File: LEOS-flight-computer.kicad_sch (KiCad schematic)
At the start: 20 parts, among them J1 MicroFit_1x4, J2 MicroFit_1x4, J3 GPIO, J4 I2C Breakout, J5 SPI Breakout, U1 MCP2562FD, U2 MCP2518FD, Y1 40 MHz

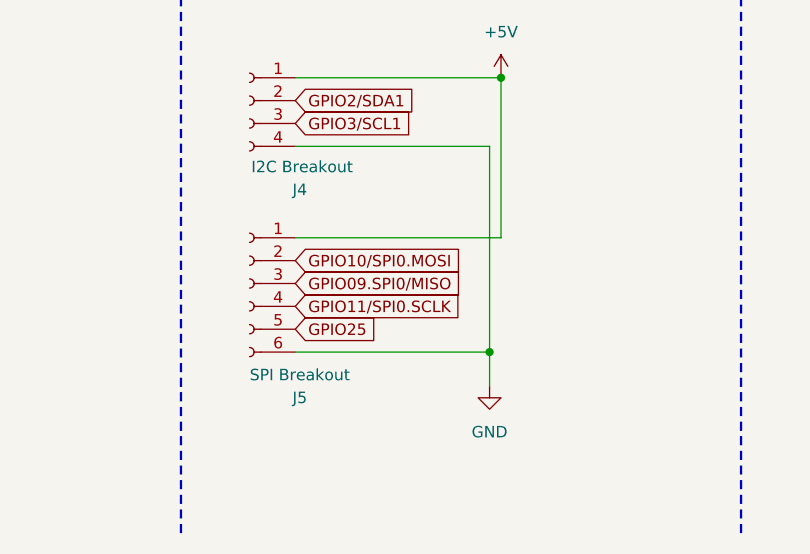
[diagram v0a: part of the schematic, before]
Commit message: Corrected layout for flight computer with breakout headers routed
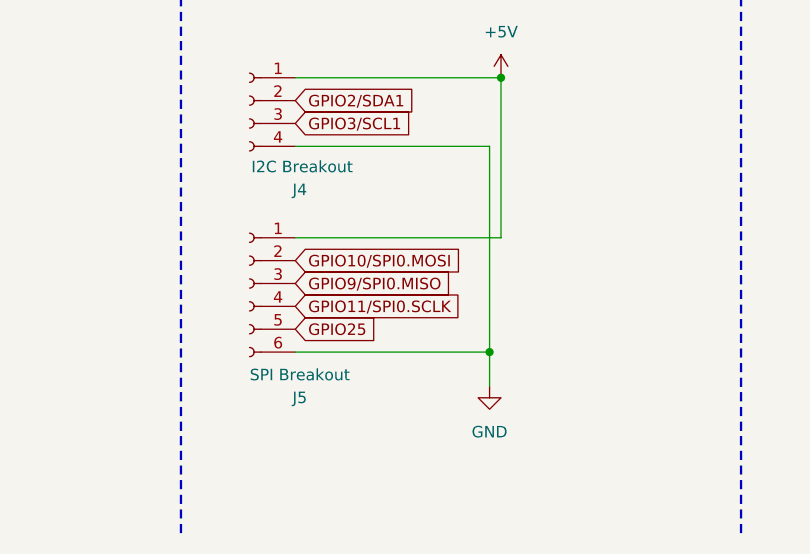
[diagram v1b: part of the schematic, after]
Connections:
- net GPIO09.SPI0/MISO is gone; now on net GPIO9/SPI0.MISO: J5.3 (Pin_3)
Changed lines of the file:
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@@
 		)
 	)
-	(global_label "GPIO09.SPI0{slash}MISO"
+	(global_label "GPIO9{slash}SPI0.MISO"
 		(shape input)
 		(at 127 170.18 0)
@@
 		)
 		(property "Intersheetrefs" "${INTERSHEET_REFS}"
-			(at 147.7048 170.18 0)
+			(at 146.4953 170.18 0)
 			(effects
 				(font

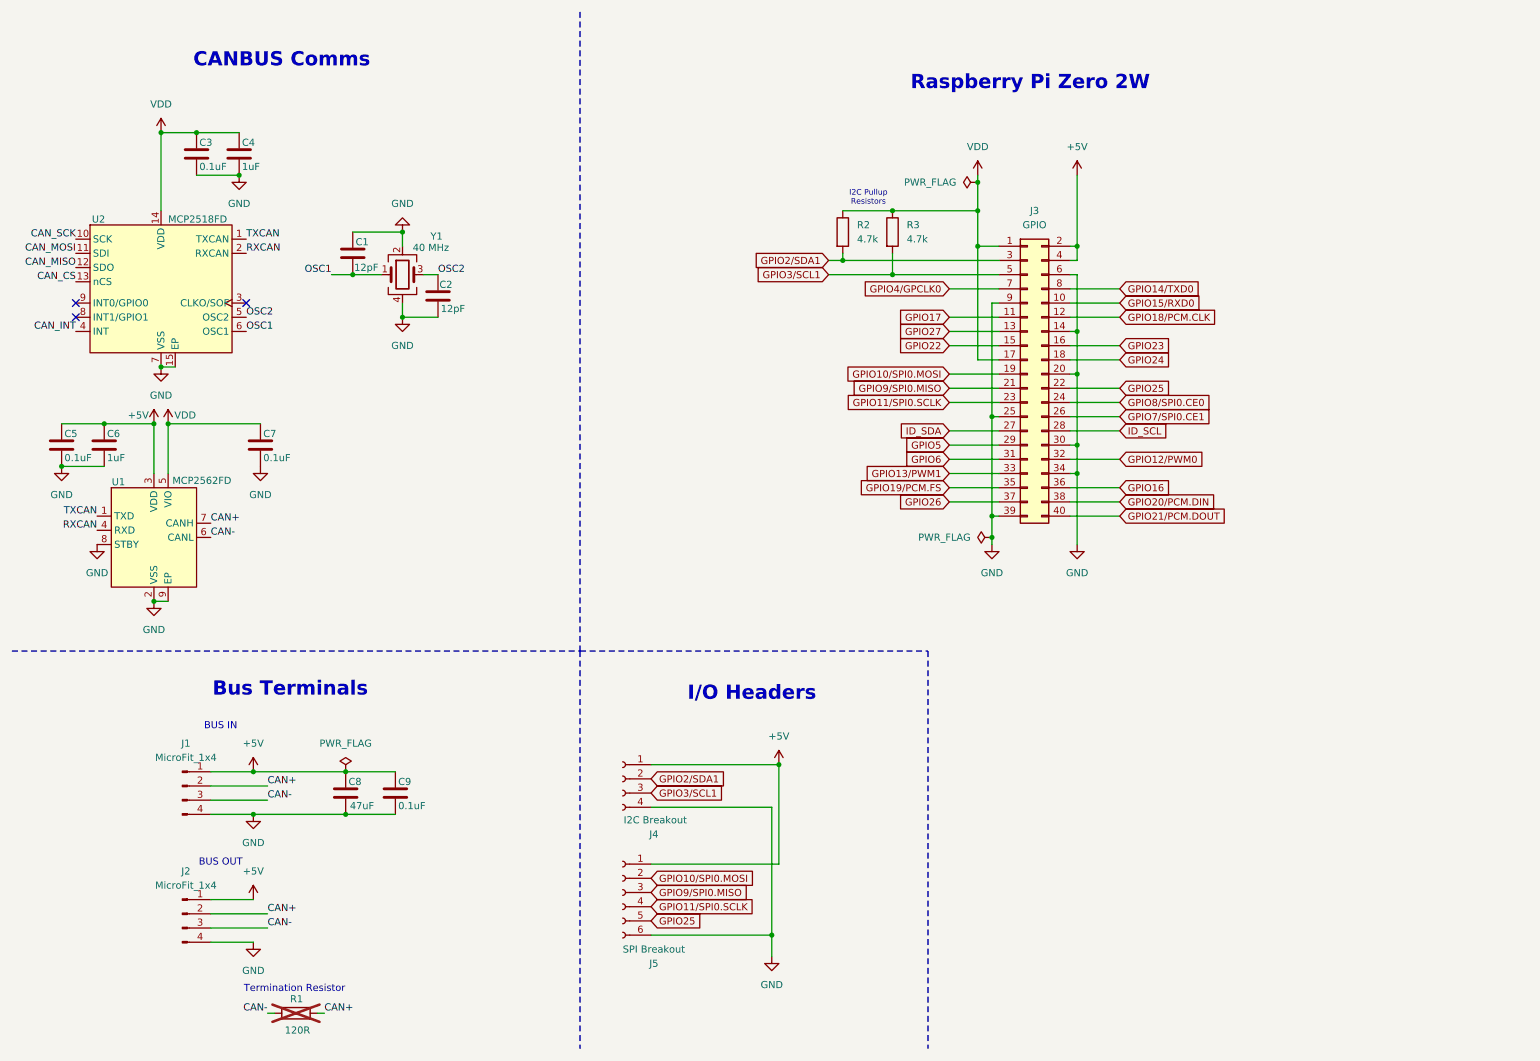
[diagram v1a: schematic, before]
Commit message: I routed and schematiced the gps model (SAM-M8Q).
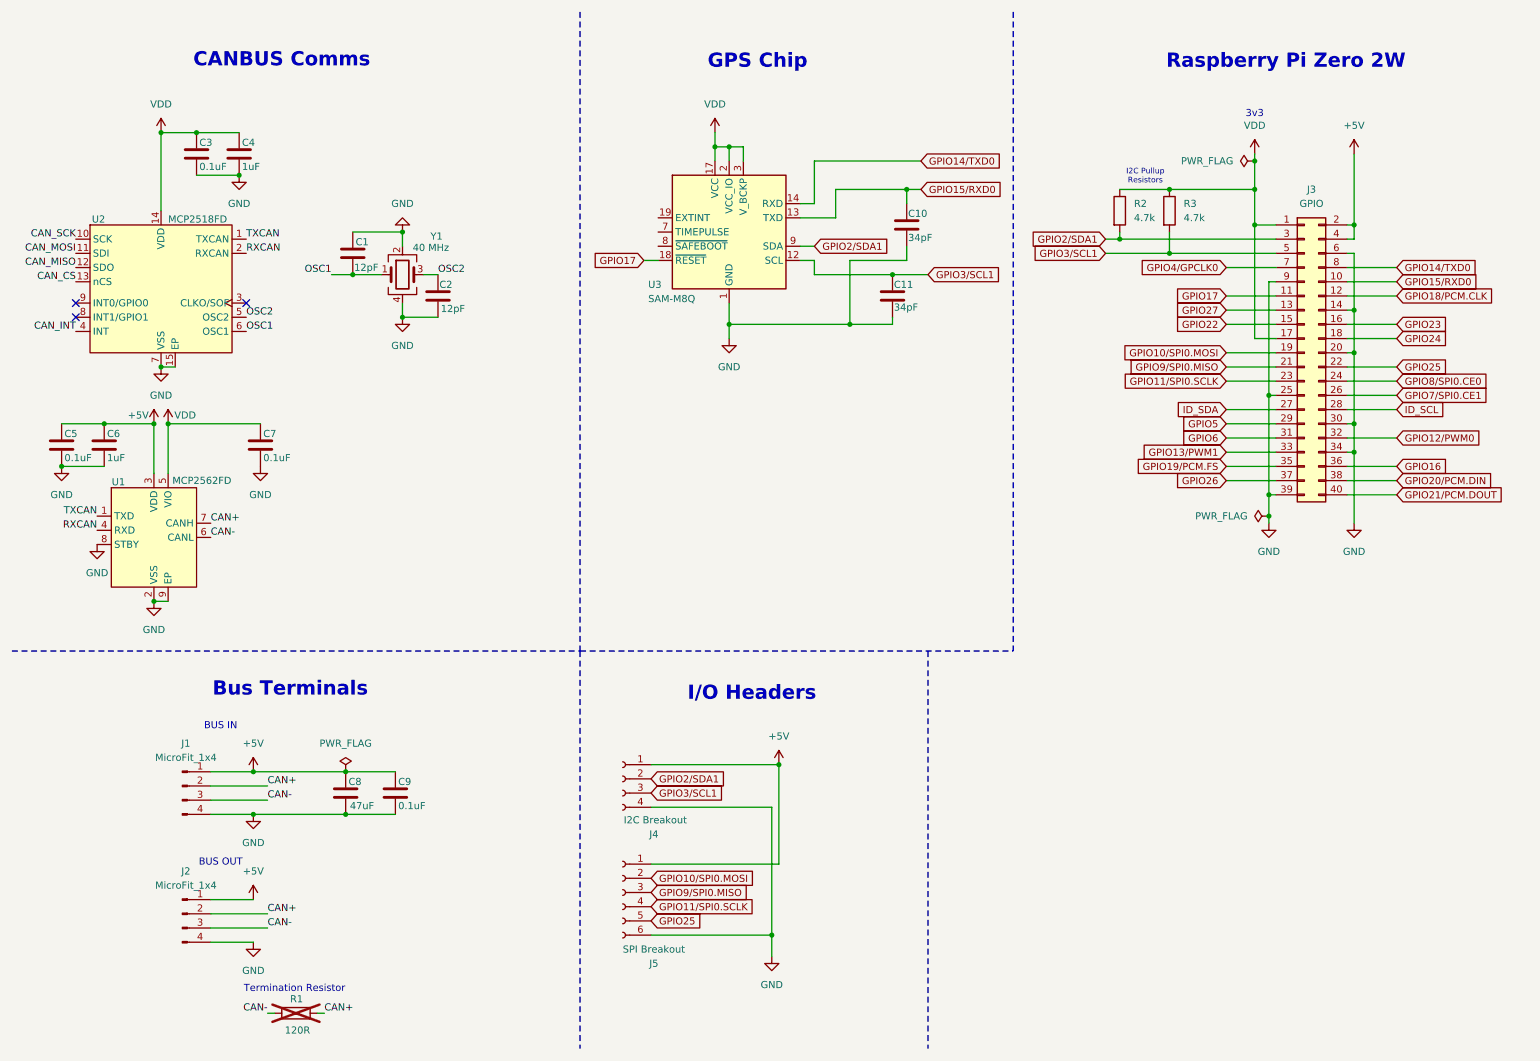
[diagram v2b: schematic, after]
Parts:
- added C10, C11: 34pF, Capacitor_SMD:C_0603_1608Metric, symbol Device:C
- added U3: SAM-M8Q, RF_GPS:ublox_SAM-M8Q, symbol RF_GPS:SAM-M8Q
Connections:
- net GND: now also C10.2, C11.2, U3.1 (GND), U3.10 (GND), U3.11 (GND), U3.15 (GND), U3.16 (GND), U3.20 (GND), U3.4 (GND), U3.5 (GND), U3.6 (GND)
- net GPIO14/TXD0: now also U3.14 (RXD)
- net GPIO15/RXD0: now also C10.1, U3.13 (TXD)
- net GPIO17: now also U3.18 (~{RESET})
- net GPIO2/SDA1: now also U3.9 (SDA)
- net GPIO3/SCL1: now also C11.1, U3.12 (SCL)
- net VDD: now also U3.17 (VCC), U3.2 (VCC_IO), U3.3 (V_BCKP)
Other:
- note added: "3v3"
- note added: "GPS Chip"
- moved on the sheet: J3, R2, R3
